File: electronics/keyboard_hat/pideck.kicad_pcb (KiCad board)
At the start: 2 copper layers, 21.3 x 52 mm, 35 parts, among them J1 Conn_01x20_Socket, J2 Conn_01x20_Socket, J3 BM20B_0.8_-34DS-0.4V_53_, Q1 RE1C002UNTCL, Q2 RE1C002UNTCL, Q3 RE1C002UNTCL, Q4 RE1C002UNTCL, Q5 RE1C002UNTCL, Q6 RE1C002UNTCL, Q7 RE1C002UNTCL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

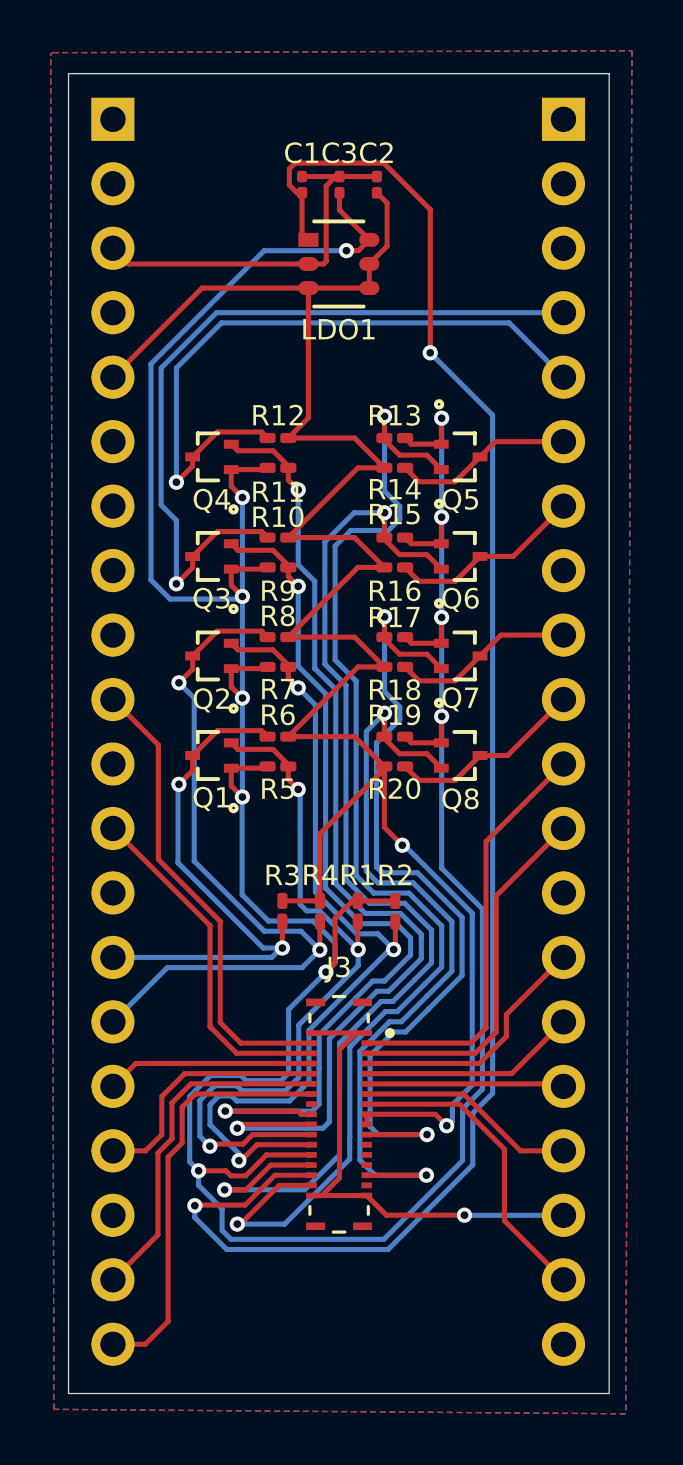
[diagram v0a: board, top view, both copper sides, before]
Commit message: updated schematic to new chip and completed layout
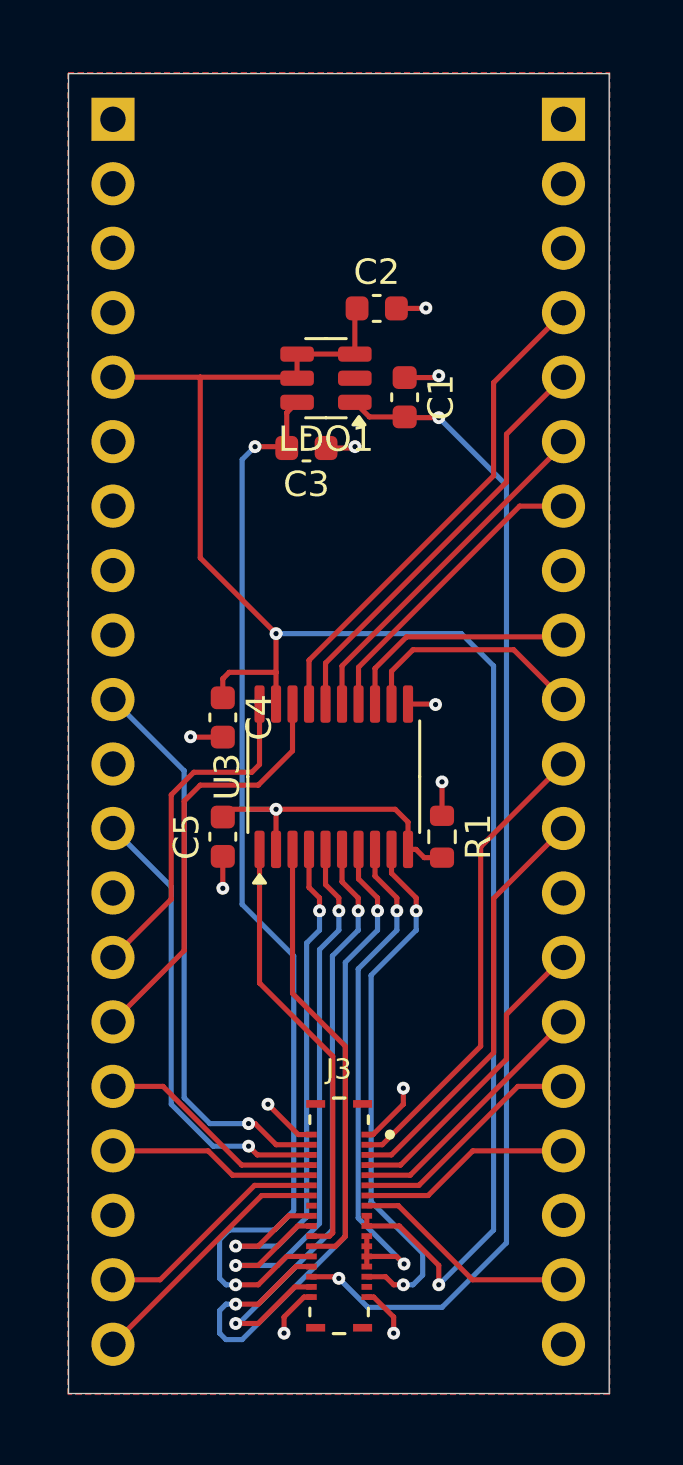
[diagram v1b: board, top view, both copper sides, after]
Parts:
- removed Q1, Q2, Q3, Q4, Q5, Q6, Q7, Q8: RE1C002UNTCL, RE1C002UNTCL:DIO_RB558WMF_ROM
- removed R10, R11, R12, R13, R14, R15, R16, R17, R18, R19, R20, R5, R6, R7, R8, R9: 10K, Resistor_SMD:R_0201_0603Metric_Pad0.64x0.40mm_HandSolder
- removed R2, R3, R4: 10k, Resistor_SMD:R_0201_0603Metric_Pad0.64x0.40mm_HandSolder
- added C4: 0.1uF, Capacitor_SMD:C_0603_1608Metric, F.Cu at (131.1, 99.4)
- added C5: 0.1uF, Capacitor_SMD:C_0603_1608Metric, F.Cu at (131.1, 104.1)
- added U3: TXS0108EPWR, Package_SO:TSSOP-20_4.4x6.5mm_P0.65mm, F.Cu at (135.4, 101.7)
- C1, C2, C3: footprint Capacitor_SMD:C_0201_0603Metric -> Capacitor_SMD:C_0603_1608Metric
- LDO1: footprint AP7312-1828W6-7:SOT26_DIO -> Package_TO_SOT_SMD:SOT-23-6
- R1: footprint Resistor_SMD:R_0201_0603Metric_Pad0.64x0.40mm_HandSolder -> Resistor_SMD:R_0603_1608Metric
- moved C3 10.5 mm to (134.4, 88.7), turned to 180 degrees
- moved C1 9.30 mm to (138.2, 86.7)
- moved C2 4.88 mm to (137.1, 83.2), turned to 0 degrees
- moved LDO1 4.53 mm to (135.1, 86.0), turned to 180 degrees
- moved R1 4.43 mm to (139.7, 104.1), turned to -90 degrees
- moved J3 4.00 mm to (135.7, 119.0)
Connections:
- J3 pad 23: unconnected-(J3-Pad23) -> KB_BLK_LED_K_1V8
- J3 pad 25: unconnected-(J3-Pad25) -> KB_BLK_LED_K_1V8
- J3 pad 27: unconnected-(J3-Pad27) -> KB_BLK_LED_K_1V8
- R1 pad 1: TP_SCL_1V8 -> GND
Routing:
- net +1V8: track 133.5 -> 56.6 mm, vias 11 -> 3
- net TP_RESET_1V8: track 48.4 -> 24.6 mm
- net +2V8: track 66.8 -> 46.4 mm
- net GND: track 35.1 -> 17.5 mm, vias 1 -> 11
- net TP_SHUTDOWN_1V8: track 39.8 -> 22.9 mm
- net TP_SDA_1V8: track 34.0 -> 17.6 mm, vias 3 -> 0
- net TP_BLK_LED_K_1V8: track 43.9 -> 28.1 mm
- net TP_MOTION_1V8: track 35.6 -> 21.6 mm
- net KB_BLK_LED_A: track 81.5 -> 68.4 mm
- net KB_BLK_LED_K_1V8: track 33.0 -> 20.9 mm
- net TP_SDA_3V3: track 28.8 -> 16.8 mm, vias 2 -> 0
- net TP_SCL_1V8: track 29.0 -> 17.2 mm, vias 3 -> 0
- net TP_MOTION_3V3: track 30.3 -> 19.6 mm, vias 1 -> 0
- net PANNEL_BLK_LED_K_1V8: track 30.8 -> 21.2 mm
- net TP_SHUTDOWN_3V3: track 26.1 -> 16.8 mm, vias 1 -> 0
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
